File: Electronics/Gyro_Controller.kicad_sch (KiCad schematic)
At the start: 35 parts, among them J3 SWCLK SWD, SW3 SW_Push, SW4 ~{USB_BOOT}, U7 W25Q32JVZP, U8 RP2040, Y2 ABM8-272-T3

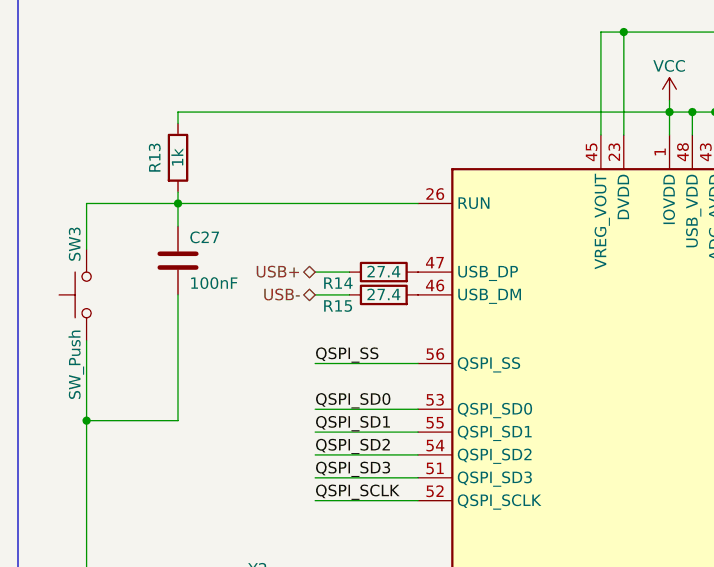
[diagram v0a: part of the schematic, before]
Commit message: USB to UART converter
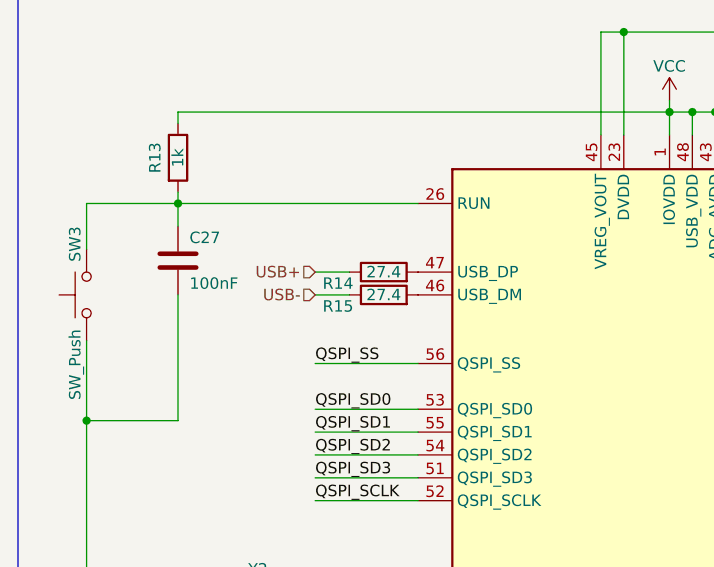
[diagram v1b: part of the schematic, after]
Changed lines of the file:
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@@
     (effects (font (size 1.27 1.27)) (justify right bottom))
   )
-  (hierarchical_label "USB+" (shape bidirectional) (at 48.26 49.53 180) (fields_autoplaced)
+  (hierarchical_label "USB+" (shape input) (at 48.26 49.53 180) (fields_autoplaced)
     (effects (font (size 1.27 1.27)) (justify right))
   )
@@
     (effects (font (size 1.27 1.27)) (justify left))
   )
-  (hierarchical_label "USB-" (shape bidirectional) (at 48.26 52.07 180) (fields_autoplaced)
+  (hierarchical_label "USB-" (shape input) (at 48.26 52.07 180) (fields_autoplaced)
     (effects (font (size 1.27 1.27)) (justify right))
   )

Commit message: power + usb
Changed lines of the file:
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@@
     (effects (font (size 1.27 1.27)) (justify right bottom))
   )
-  (hierarchical_label "USB+" (shape input) (at 48.26 49.53 180) (fields_autoplaced)
+  (hierarchical_label "USB+" (shape bidirectional) (at 48.26 49.53 180) (fields_autoplaced)
     (effects (font (size 1.27 1.27)) (justify right))
   )
@@
     (effects (font (size 1.27 1.27)) (justify left))
   )
-  (hierarchical_label "USB-" (shape input) (at 48.26 52.07 180) (fields_autoplaced)
+  (hierarchical_label "USB-" (shape bidirectional) (at 48.26 52.07 180) (fields_autoplaced)
     (effects (font (size 1.27 1.27)) (justify right))
   )
